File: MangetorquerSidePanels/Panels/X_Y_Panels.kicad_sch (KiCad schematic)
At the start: 89 parts, among them J1 Through_Hole_1, J2 MOLEX_2053380006, J3 Through_Hole_1, J4 Through_Hole_1, J5 Through_Hole_1, J6 Through_Hole_1, Q1 BSS138DWQ-7, Q2 MBT2222ADW1T1, Q3 BSS138DWQ-7, Q4 MBT2222ADW1T1, U1 DRV8830DGQ, U2 BD60GC0WEFJ, U3 OPT3001

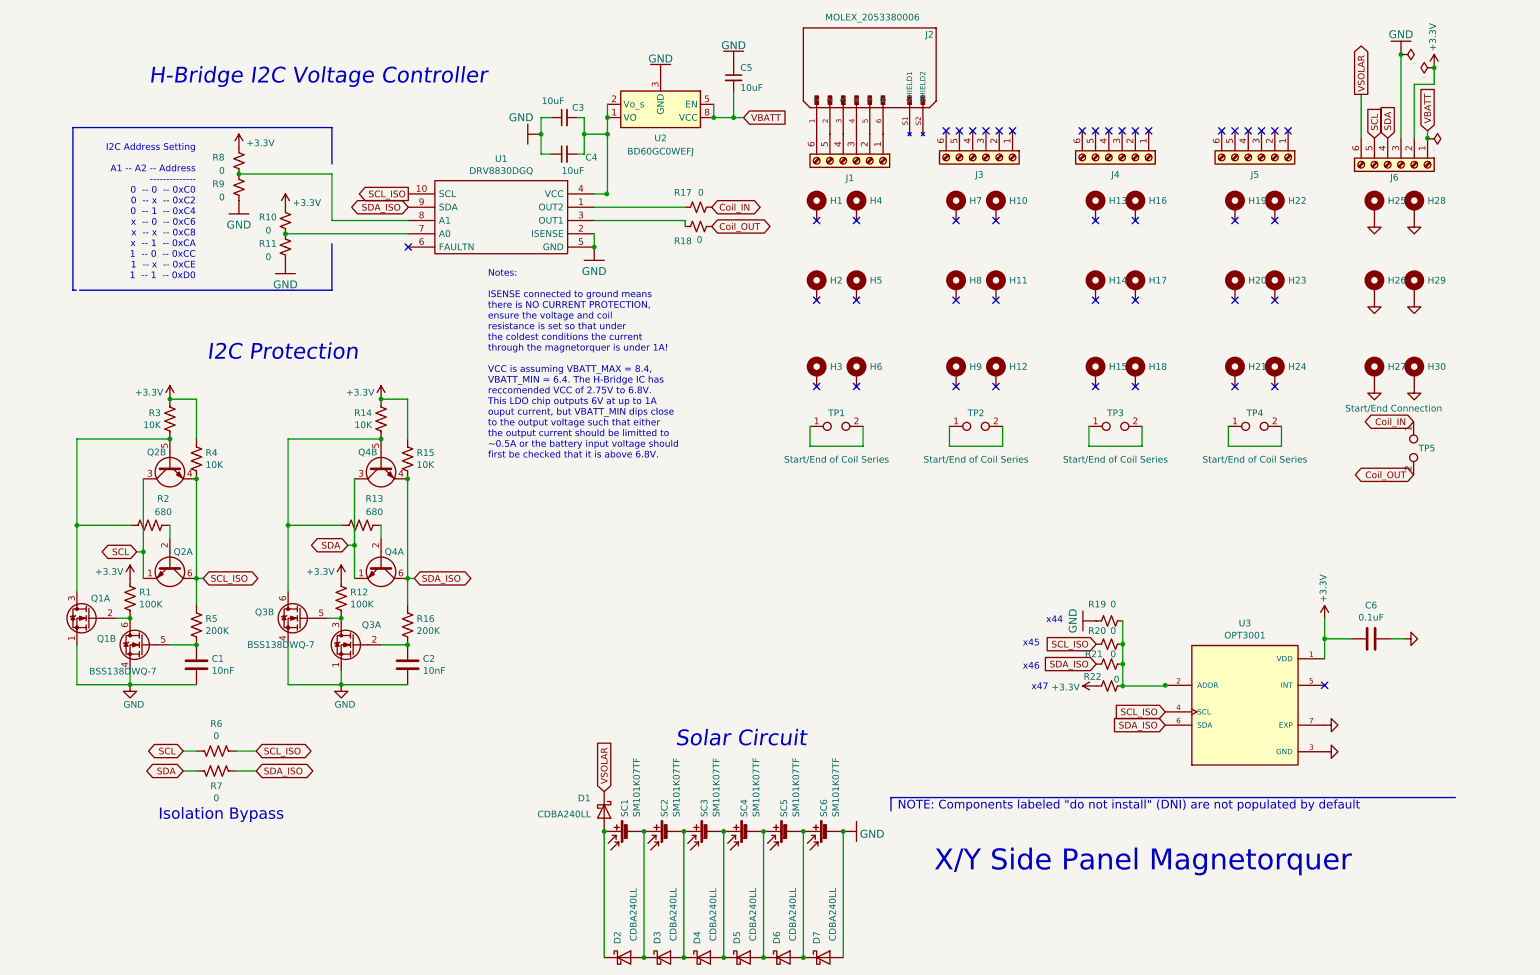
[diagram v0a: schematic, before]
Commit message: deleted extra holes in schematic
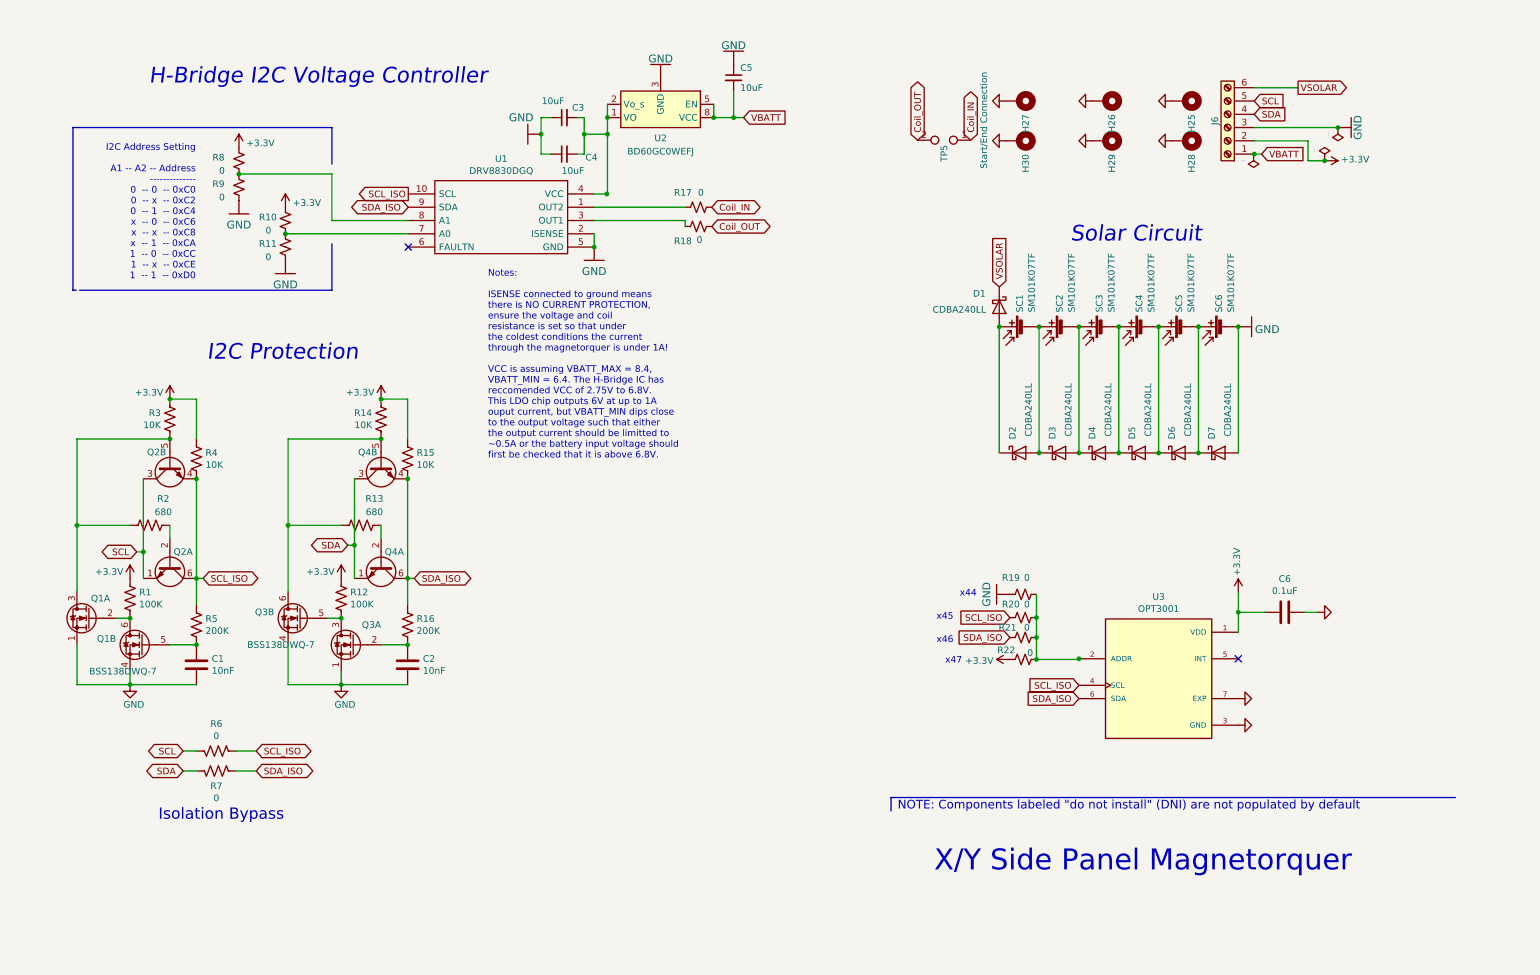
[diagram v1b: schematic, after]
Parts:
- removed H1, H10, H11, H12, H13, H14, H15, H16, H17, H18, H19, H2, H20, H21, H22, H23, H24, H3, H4, H5, H6, H7, H8, H9: ~, MountingHole:MountingHole_2.2mm_M2_DIN965_Pad_TopBottom, symbol Mechanical:MountingHole_Pad
- removed J1, J3, J4, J5: Through_Hole_1, Connector_PinHeader_2.54mm:PinHeader_1x06_P2.54mm_Vertical, symbol Connector:Screw_Terminal_01x06
- removed J2: MOLEX_2053380006, panels:MOLEX_2053380006, symbol solar-panel-side-X-plus-rescue:2053380006-sapling
- removed TP1, TP2, TP3, TP4: Start/End of Coil Series, panels:TestPointConnection, symbol Connector:TestPoint_2Pole
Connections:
- no-connect marks 44 -> 2
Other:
- moved on the sheet: C6, D1, D2, D3, D4, D5, D6, D7, H25, H26, H27, H28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

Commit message: Final flight side panels w/ magnetorquers finished, note final board thickness of 0.031'' and updated copper weight of 0.5oz for internal layers
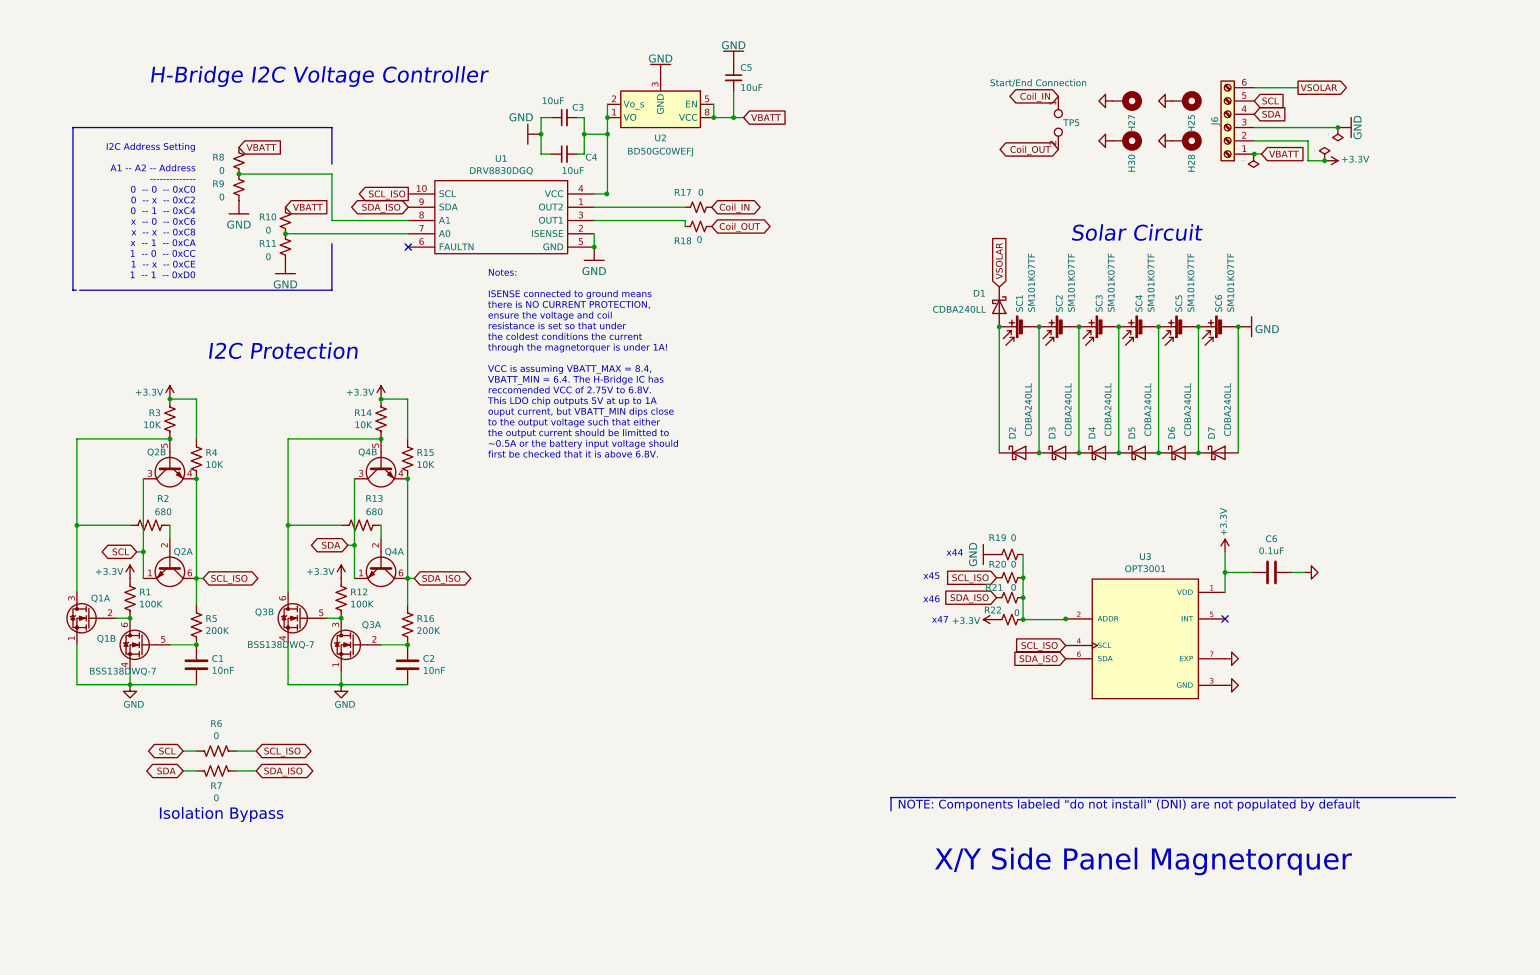
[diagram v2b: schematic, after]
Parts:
- removed H26, H29: ~, MountingHole:MountingHole_2.2mm_M2_DIN965_Pad_TopBottom, symbol Mechanical:MountingHole_Pad
- U2: value BD60GC0WEFJ -> BD50GC0WEFJ
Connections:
- net +3V3: no longer R10.1, R8.1
- net VBATT: now also R10.1, R8.1
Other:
- note added: "Notes: ISENSE connected to ground means there is NO CURRENT PROTECTION, ensure the voltage and coil resistance is set so that under the coldest conditions the current through the magnetorquer is under 1A! VCC is assuming VBATT_MAX = 8.4, VBATT_MIN = 6.4. The H-Bridge IC has reccomended VCC of 2.75V to 6.8V. This LDO chip outputs 5V at up to 1A ouput current, but VBATT_MIN dips close to the output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"
- note removed: "Notes: ISENSE connected to ground means there is NO CURRENT PROTECTION, ensure the voltage and coil resistance is set so that under the coldest conditions the current through the magnetorquer is under 1A! VCC is assuming VBATT_MAX = 8.4, VBATT_MIN = 6.4. The H-Bridge IC has reccomended VCC of 2.75V to 6.8V. This LDO chip outputs 6V at up to 1A ouput current, but VBATT_MIN dips close to the output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"
- moved on the sheet: C6, H27, H30, R19, R20, R21, R22, TP5, U3

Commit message: added magnetorquers
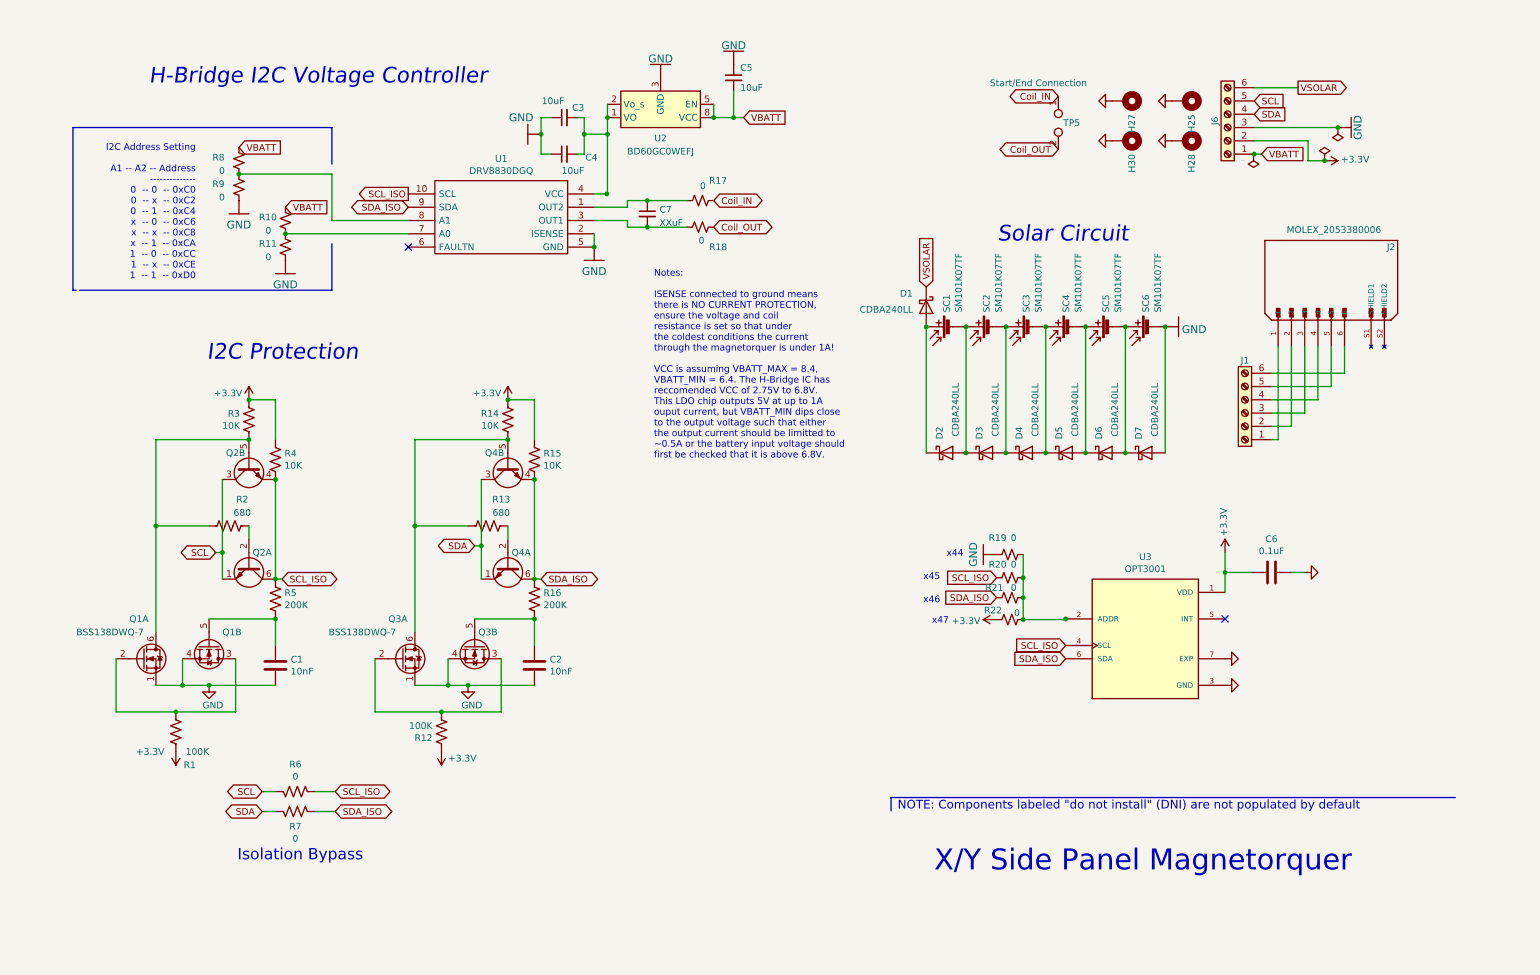
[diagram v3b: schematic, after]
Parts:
- removed Q1, Q3: BSS138DWQ-7, panels:BSS138DWQ-7, symbol xpanel-rescue:BSS138DWQ-7-symbols
- added C7: XXuF, Capacitor_SMD:C_1210_3225Metric, symbol Device:C_Small
- added J1: Through_Hole_1, Connector_PinHeader_2.54mm:PinHeader_1x06_P2.54mm_Vertical, symbol Connector:Screw_Terminal_01x06
- added J2: MOLEX_2053380006, panels:MOLEX_2053380006, symbol solar-panel-side-X-plus-rescue:2053380006-sapling
- added Q1, Q3: BSS138DWQ-7, panels:BSS138DWQ-7, symbol Sapling_Side_Panels:BSS138DWQ-7
- U2: value BD50GC0WEFJ -> BD60GC0WEFJ
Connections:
- net GND: now also Q1.1 (S2), Q1.4 (S1), Q3.1 (S2), Q3.4 (S1)
- net at C2.1, R16.1: now also Q3.5 (G1)
- net at R17.1, U1.1 (OUT2): now also C7.1
- net at R12.1: now also Q3.2 (G2), Q3.3 (D2)
- net at R18.1, U1.3 (OUT1): now also C7.2
- net at C1.1, R5.1: now also Q1.5 (G1)
- net at Q2.5 (B2), R2.1, R3.2: now also Q1.6 (D1)
- net at Q4.5 (B2), R13.2, R14.2: now also Q3.6 (D1)
- net at R1.1: now also Q1.2 (G2), Q1.3 (D2)
- new net: J1.1 (Pin_1), J2.1
- new net: J1.2 (Pin_2), J2.2
- new net: J1.3 (Pin_3), J2.3
- new net: J1.4 (Pin_4), J2.4
- new net: J1.5 (Pin_5), J2.5
- new net: J1.6 (Pin_6), J2.6
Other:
- moved on the sheet: C1, C2, D1, D2, D3, D4, D5, D6, D7, Q2A, Q2B, Q4A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
